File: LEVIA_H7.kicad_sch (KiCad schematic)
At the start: 8 parts, among them U1 USBLC6-2P6

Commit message: MORE LAYOUT TESTS
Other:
- sheet DIGITAL VTX ports: added UART4{UART}; removed UART2{UART}
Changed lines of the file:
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@@
+		)
+	)
+	(bus
+		(pts
+			(xy 170.18 66.04) (xy 187.96 66.04)
+		)
+		(stroke
+			(width 0)
+			(type default)
 		)
 	)
@@
 		(pts
 			(xy 129.54 175.26) (xy 129.54 176.53)
-		)
-		(stroke
-			(width 0)
-			(type default)
-		)
-	)
-	(bus
-		(pts
-			(xy 170.18 66.04) (xy 187.96 66.04)
 		)
 		(stroke
@@
 		)
 		(pin "UART2{UART}" input
-			(at 170.18 66.04 0)
-			(effects
-				(font
-					(size 1.27 1.27)
-				)
-				(justify right)
+			(at 120.65 63.5 180)
+			(effects
+				(font
+					(size 1.27 1.27)
+				)
+				(justify left)
 			)
 		)
@@
 		)
 		(pin "UART4{UART}" input
-			(at 120.65 66.04 180)
-			(effects
-				(font
-					(size 1.27 1.27)
-				)
-				(justify left)
+			(at 170.18 66.04 0)
+			(effects
+				(font
+					(size 1.27 1.27)
+				)
+				(justify right)
 			)
 		)
@@
 			)
 		)
-		(pin "UART2{UART}" bidirectional
-			(at 187.96 66.04 180)
-			(effects
-				(font
-					(size 1.27 1.27)
-				)
-				(justify left)
-			)
-		)
 		(pin "UART3{UART}" input
 			(at 187.96 68.58 180)
 			(effects
 				(font
+					(size 1.27 1.27)
+				)
+				(justify left)
+			)
+		)
+		(pin "UART4{UART}" input
+			(at 187.96 66.04 180)
+			(effects
+				(font

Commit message: more layout
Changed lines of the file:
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@@
 		)
 		(pin "UART2{UART}" input
-			(at 120.65 63.5 180)
+			(at 120.65 66.04 180)
 			(effects
 				(font

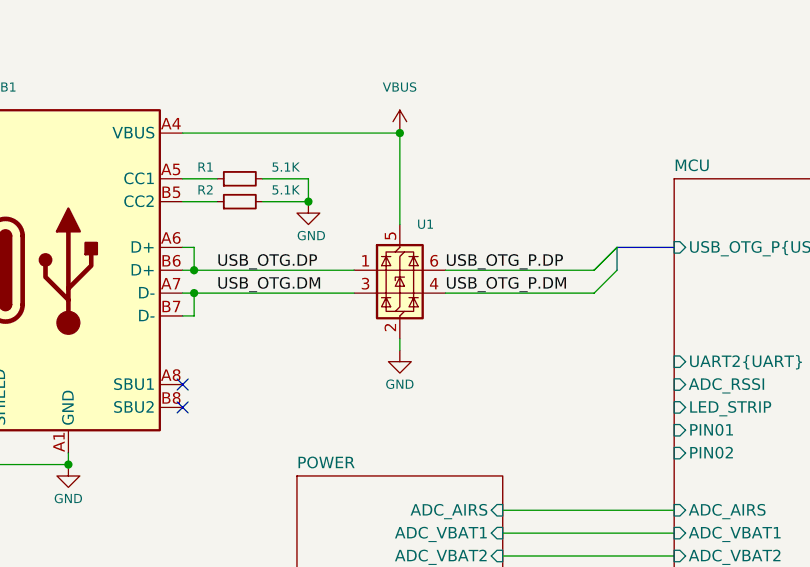
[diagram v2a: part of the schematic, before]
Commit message: fix usb diff pair suffix
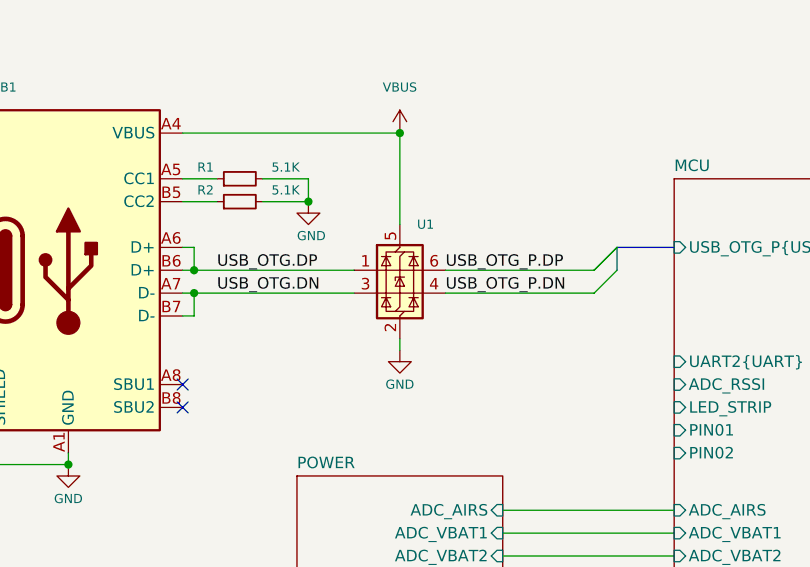
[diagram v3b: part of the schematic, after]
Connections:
- net USB_OTG.DM renamed USB_OTG.DN
- net USB_OTG_P.DM renamed USB_OTG_P.DN
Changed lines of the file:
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@@
 		)
 	)
-	(label "USB_OTG.DM"
+	(label "USB_OTG.DN"
 		(at 69.85 58.42 0)
 		(effects
@@
 		)
 	)
-	(label "USB_OTG_P.DM"
+	(label "USB_OTG_P.DN"
 		(at 95.25 58.42 0)
 		(effects

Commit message: PDN
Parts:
- H1, H2, H3, H4: footprint MountingHole:MountingHole_3.2mm_M3_DIN965_Pad_TopBottom -> _pico:MountingHole_3.2mm_M3_ISO14580_Pad_TopBottom; now fitted
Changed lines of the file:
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@@
 		(exclude_from_sim no)
 		(in_bom no)
-		(on_board no)
+		(on_board yes)
 		(in_pos_files no)
-		(dnp yes)
+		(dnp no)
 		(fields_autoplaced yes)
 		(property "Reference" "H2"
@@
 			)
 		)
-		(property "Footprint" "MountingHole:MountingHole_3.2mm_M3_DIN965_Pad_TopBottom"
+		(property "Footprint" "_pico:MountingHole_3.2mm_M3_ISO14580_Pad_TopBottom"
 			(at 114.3 172.72 0)
 			(hide yes)
@@
 		(exclude_from_sim no)
 		(in_bom no)
-		(on_board no)
+		(on_board yes)
 		(in_pos_files no)
-		(dnp yes)
+		(dnp no)
 		(fields_autoplaced yes)
 		(property "Reference" "H1"
@@
 			)
 		)
-		(property "Footprint" "MountingHole:MountingHole_3.2mm_M3_DIN965_Pad_TopBottom"
+		(property "Footprint" "_pico:MountingHole_3.2mm_M3_ISO14580_Pad_TopBottom"
 			(at 106.68 172.72 0)
 			(hide yes)
@@
 		(exclude_from_sim no)
 		(in_bom no)
-		(on_board no)
+		(on_board yes)
 		(in_pos_files no)
-		(dnp yes)
+		(dnp no)
 		(fields_autoplaced yes)
 		(property "Reference" "H3"
@@
 			)
 		)
-		(property "Footprint" "MountingHole:MountingHole_3.2mm_M3_DIN965_Pad_TopBottom"
+		(property "Footprint" "_pico:MountingHole_3.2mm_M3_ISO14580_Pad_TopBottom"
 			(at 121.92 172.72 0)
 			(hide yes)
@@
 		(exclude_from_sim no)
 		(in_bom no)
-		(on_board no)
+		(on_board yes)
 		(in_pos_files no)
-		(dnp yes)
+		(dnp no)
 		(fields_autoplaced yes)
 		(property "Reference" "H4"
@@
 			)
 		)
-		(property "Footprint" "MountingHole:MountingHole_3.2mm_M3_DIN965_Pad_TopBottom"
+		(property "Footprint" "_pico:MountingHole_3.2mm_M3_ISO14580_Pad_TopBottom"
 			(at 129.54 172.72 0)
 			(hide yes)
@@
 		(size 22.86 12.7)
 		(exclude_from_sim no)
-		(in_bom no)
-		(on_board no)
-		(dnp yes)
+		(in_bom yes)
+		(on_board yes)
+		(dnp no)
 		(fields_autoplaced yes)
 		(stroke
